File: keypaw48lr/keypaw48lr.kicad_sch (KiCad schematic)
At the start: 109 parts, among them J1 Conn_01x02, J2 Conn_01x02, J3 Conn_01x02, J4 Conn_01x02, J5 Conn_01x02, J6 JD9613_OLED_FPC_Conn_01x10, J7 JD9613_OLED_FPC_Conn_01x10, SW1 SW_SPDT, SW2 RotaryEncoder, U1 nice_nano, U2 PAW3395, U3 TLV70019_SOT23-5, U4 TPS22917DBV

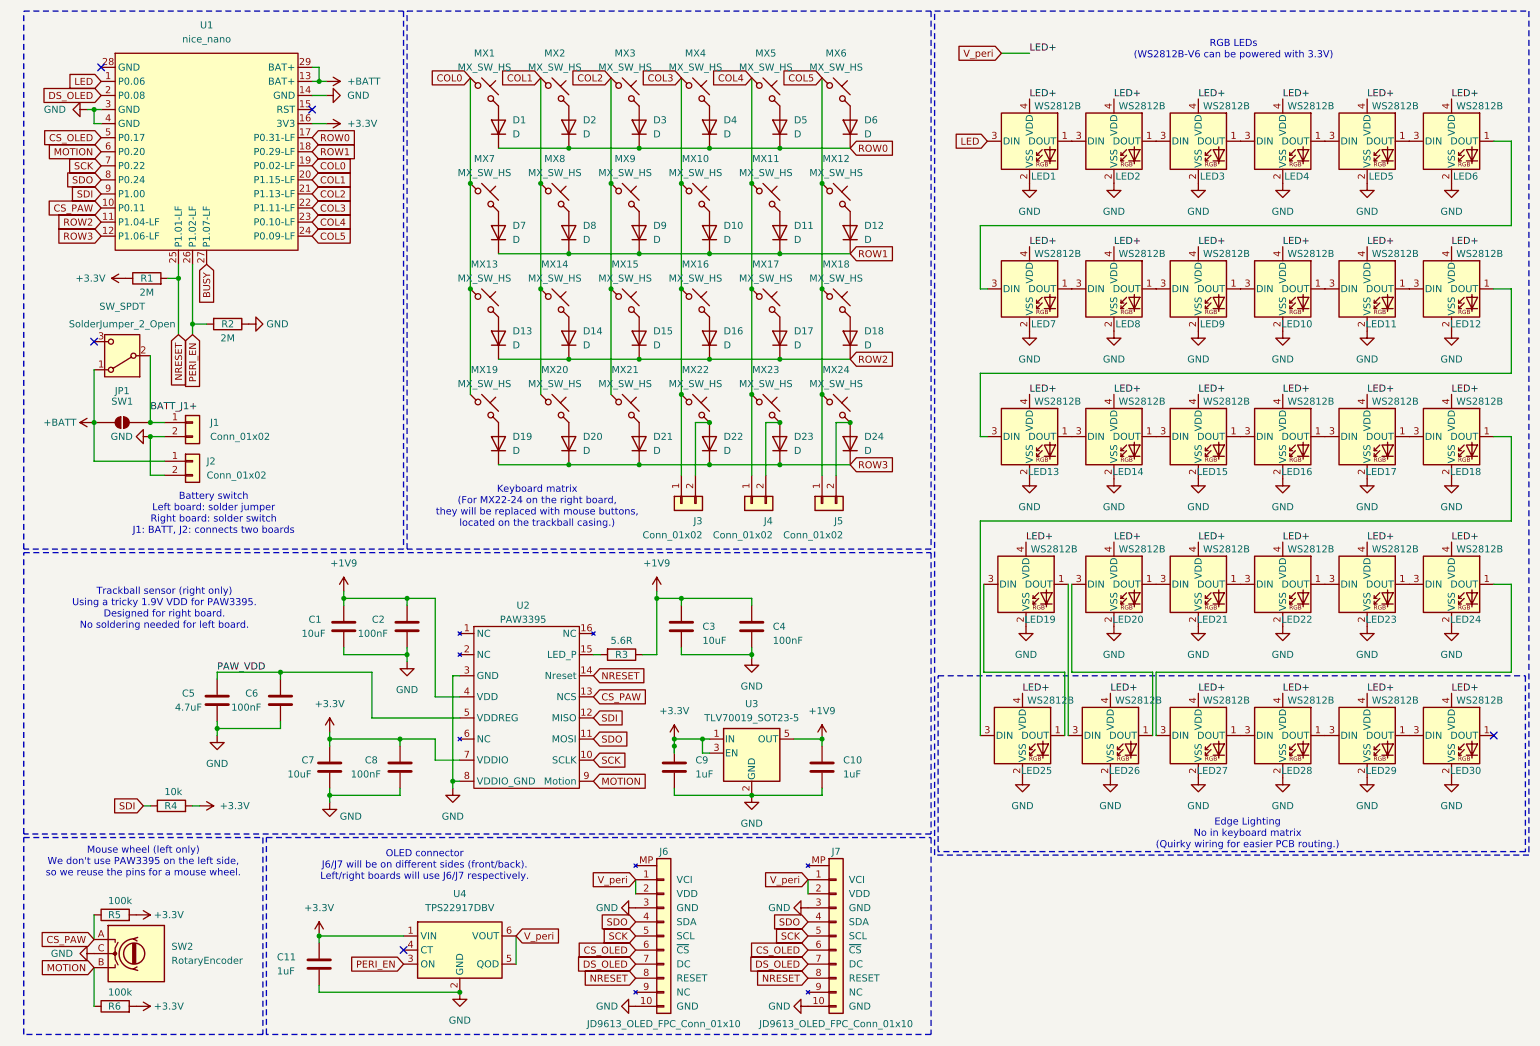
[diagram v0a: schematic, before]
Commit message: feat: replace encoder with a touch bar
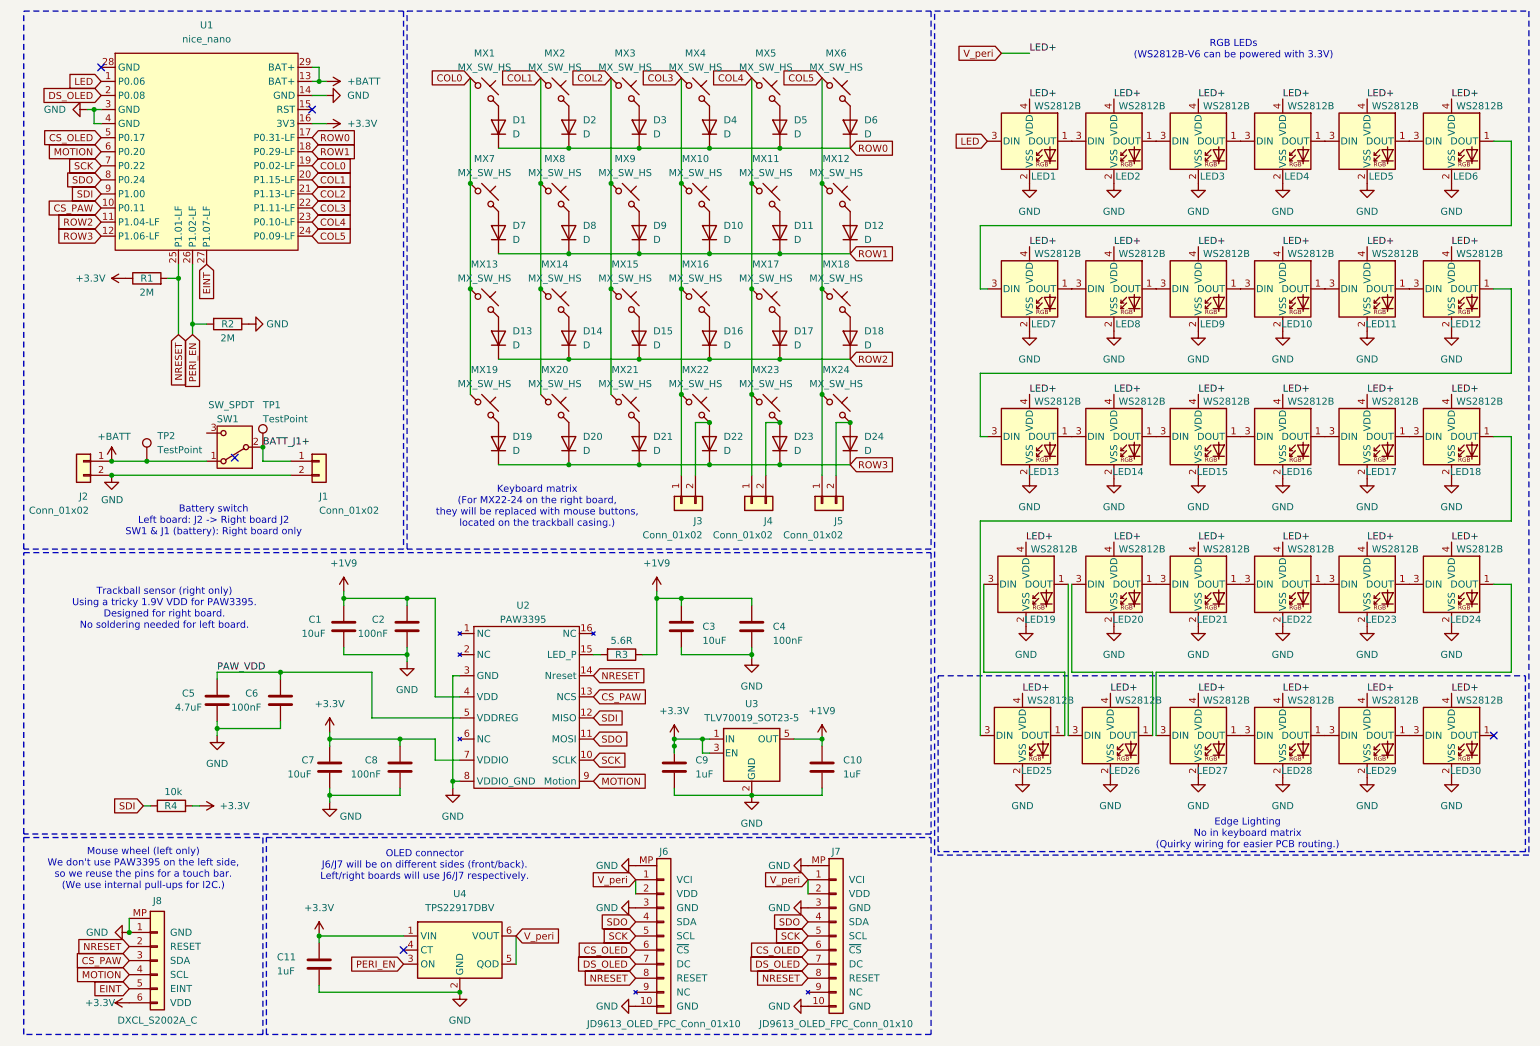
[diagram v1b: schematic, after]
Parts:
- removed JP1: SolderJumper_2_Open, Jumper:SolderJumper-2_P1.3mm_Open_TrianglePad1.0x1.5mm, symbol Jumper:SolderJumper_2_Open
- removed R5, R6: 100k, Resistor_SMD:R_1206_3216Metric_Pad1.30x1.75mm_HandSolder, symbol Device:R
- removed SW2: RotaryEncoder, ALPS_EC10E:RotaryEncoder_Alps_EC10E-Switch, symbol Device:RotaryEncoder
- added J8: DXCL_S2002A_C, DXCL_S2002A_C:FH34SRJ-10S-0.5SH, symbol DXCL_S2002A_C:DXCL_S2002A_C
- added TP1, TP2: TestPoint, MX_SW_HS_REV:TestPoint_THTPad_D2.0mm_Drill1.0mm_nosilk, symbol Connector:TestPoint
- D1, D10, D11, D12, D13, D14, D15, D16, D17, D18, D19, D2, D20, D21, D22, D23, D24, D3, D4, D5, D6, D7, D8, D9: footprint MX_SW_HS_REV:D_SOD-323_HandSoldering_REV -> MX_SW_HS_REV:D_SOD-123_REV
- J6, J7: footprint JD9613_OLED_FPC:TE_1-1734839-0_1x10-1MP_P0.5mm_Horizontal -> JD9613_OLED_FPC:FH34SRJ-10S-0.5SH
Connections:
- net +3.3V: now also J8.6 (VDD)
- net +BATT: now also TP2.1
- net BATT_J1+: now also TP1.1
- net CS_PAW: now also J8.3 (SDA)
- net GND: now also J6.MP, J7.MP, J8.1 (GND), J8.MP
- net MOTION: now also J8.4 (SCL)
- net NRESET: now also J8.2 (RESET)
- net BUSY renamed EINT
- net EINT: now also J8.5 (EINT)
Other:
- note added: "Battery switch Left board: J2 -> Right board J2 SW1 & J1 (battery): Right board only"
- note added: "Mouse wheel (left only) We don't use PAW3395 on the left side, so we reuse the pins for a touch bar. (We use internal pull-ups for I2C.)"
- note removed: "Battery switch Left board: solder jumper Right board: solder switch J1: BATT, J2: connects two boards"
- note removed: "Mouse wheel (left only) We don't use PAW3395 on the left side, so we reuse the pins for a mouse wheel."
- moved on the sheet: J1, J2, SW1

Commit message: feat: modify pcb for a simple box casing
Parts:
- added H1, H2, H3, H4, H5, H6, H7, H8: MountingHole, MountingHole:MountingHole_2.2mm_M2_DIN965_Pad_TopBottom, symbol Mechanical:MountingHole

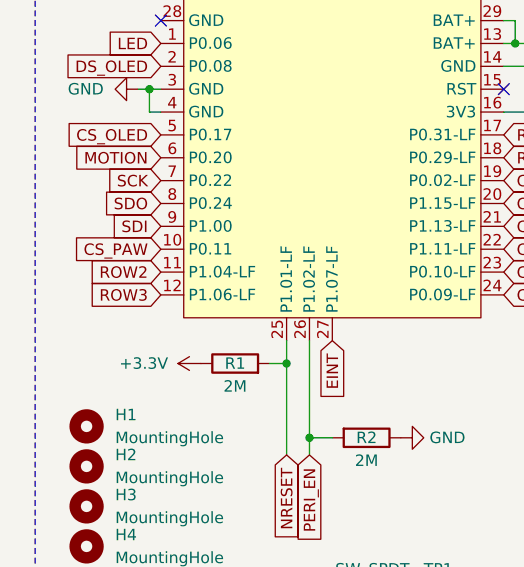
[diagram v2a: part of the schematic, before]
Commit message: fix: reversible +BATT connector for left board
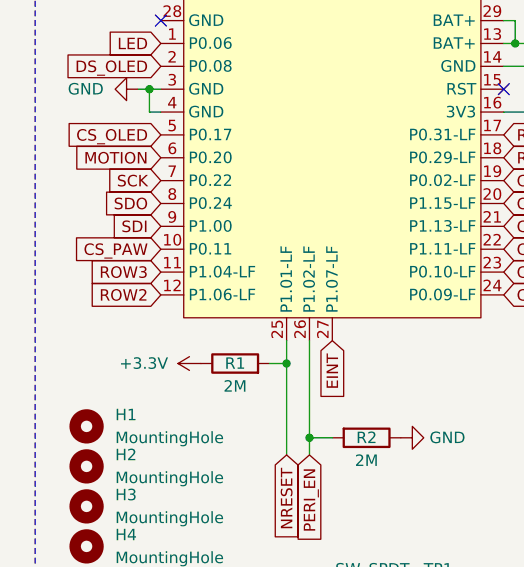
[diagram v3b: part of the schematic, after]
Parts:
- J1: footprint Connector_Molex:Molex_PicoBlade_53048-0210_1x02_P1.25mm_Horizontal -> MX_SW_HS_REV:Conn_1x02_P1.25mm_Horizontal_Battery
- J2: footprint Connector_Molex:Molex_PicoBlade_53048-0210_1x02_P1.25mm_Horizontal -> MX_SW_HS_REV:Conn_1x02_P1.25mm_Horizontal_Battery_REV
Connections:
- net ROW2: now also U1.12 (P1.06-LF); no longer U1.11 (P1.04-LF)
- net ROW3: now also U1.11 (P1.04-LF); no longer U1.12 (P1.06-LF)
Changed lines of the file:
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@@
 	(global_label "ROW2"
 		(shape input)
-		(at 26.67 50.8 180)
+		(at 26.67 53.34 180)
 		(fields_autoplaced yes)
 		(effects
@@
 		)
 		(property "Intersheetrefs" "${INTERSHEET_REFS}"
-			(at 18.4234 50.8 0)
+			(at 18.4234 53.34 0)
 			(hide yes)
 			(show_name no)
@@
 	(global_label "ROW3"
 		(shape input)
-		(at 26.67 53.34 180)
+		(at 26.67 50.8 180)
 		(fields_autoplaced yes)
 		(effects
@@
 		)
 		(property "Intersheetrefs" "${INTERSHEET_REFS}"
-			(at 18.4234 53.34 0)
+			(at 18.4234 50.8 0)
 			(hide yes)
 			(show_name no)
@@
 			)
 		)
-		(property "Footprint" "Connector_Molex:Molex_PicoBlade_53048-0210_1x02_P1.25mm_Horizontal"
+		(property "Footprint" "MX_SW_HS_REV:Conn_1x02_P1.25mm_Horizontal_Battery_REV"
 			(at 23.495 93.98 0)
 			(hide yes)
@@
 			)
 		)
-		(property "Footprint" "Connector_Molex:Molex_PicoBlade_53048-0210_1x02_P1.25mm_Horizontal"
+		(property "Footprint" "MX_SW_HS_REV:Conn_1x02_P1.25mm_Horizontal_Battery"
 			(at 66.04 93.98 0)
 			(hide yes)

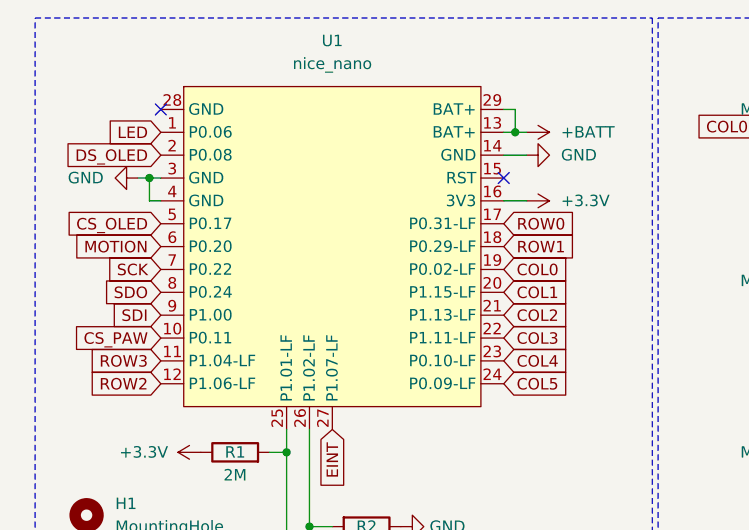
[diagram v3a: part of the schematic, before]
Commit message: fix: move oled fpc out of antenna range?
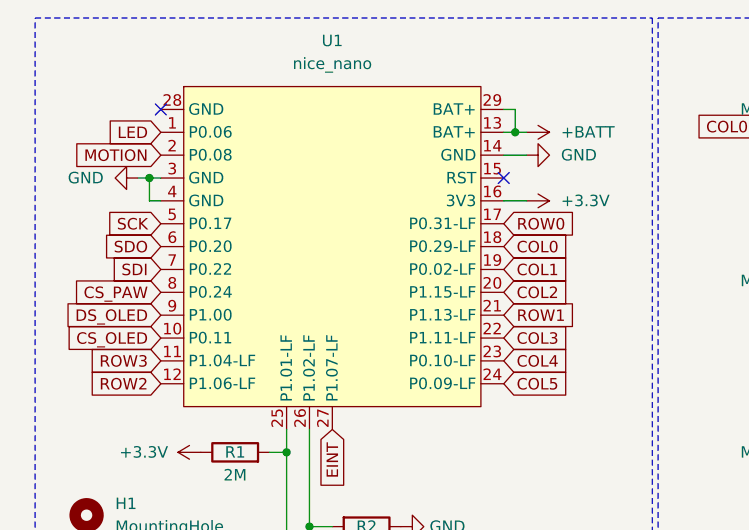
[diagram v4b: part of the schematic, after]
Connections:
- net COL0: now also U1.18 (P0.29-LF); no longer U1.19 (P0.02-LF)
- net COL1: now also U1.19 (P0.02-LF); no longer U1.20 (P1.15-LF)
- net COL2: now also U1.20 (P1.15-LF); no longer U1.21 (P1.13-LF)
- net CS_OLED: now also U1.10 (P0.11); no longer U1.5 (P0.17)
- net CS_PAW: now also U1.8 (P0.24); no longer U1.10 (P0.11)
- net DS_OLED: now also U1.9 (P1.00); no longer U1.2 (P0.08)
- net MOTION: now also U1.2 (P0.08); no longer U1.6 (P0.20)
- net ROW1: now also U1.21 (P1.13-LF); no longer U1.18 (P0.29-LF)
- net SCK: now also U1.5 (P0.17); no longer U1.7 (P0.22)
- net SDI: now also U1.7 (P0.22); no longer U1.9 (P1.00)
- net SDO: now also U1.6 (P0.20); no longer U1.8 (P0.24)

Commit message: fix: non-reverse-mountable V_peri components
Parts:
- removed J7: JD9613_OLED_FPC_Conn_01x10, JD9613_OLED_FPC:FH34SRJ-10S-0.5SH, symbol JD9613_OLED_FPC:JD9613_OLED_FPC_Conn_01x10
- added C11: 1uF, Capacitor_SMD:C_1206_3216Metric_Pad1.33x1.80mm_HandSolder, symbol Device:C
- added C12: 10uF, Capacitor_SMD:C_1206_3216Metric_Pad1.33x1.80mm_HandSolder, symbol Device:C
- C13: renamed from C11; footprint Capacitor_SMD:C_1206_3216Metric_Pad1.33x1.80mm_HandSolder -> MX_SW_HS_REV:C_1206_3216Metric_Pad1.33x1.80mm_HandSolder_REV
- renumbered J2 to J1, J1 to J2, J8 to J7
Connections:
- net GND: now also C11.2, C12.2
- net V_peri: now also C11.1, C12.1
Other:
- note added: "OLED connector Left/right boards will share the same J6 due to the asymmetry in the OLED FPC."
- note removed: "OLED connector J6/J7 will be on different sides (front/back). Left/right boards will use J6/J7 respectively."
- moved on the sheet: J6
